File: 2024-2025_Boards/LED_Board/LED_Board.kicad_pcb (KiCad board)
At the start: 2 copper layers, 40 parts, among them J1 Conn_01x02_Socket, J2 Conn_01x02_Socket, J3 Conn_ARM_JTAG_SWD_10, J4 Conn_01x03_Socket, J5 Conn_01x03_Socket, J6 Conn_01x02_Pin, J7 Conn_01x02_Pin, U1 AMS1117-5.0, U2 AMS1117-3.3, U3 MCP2562-E-P, U4 STM32G474RETx

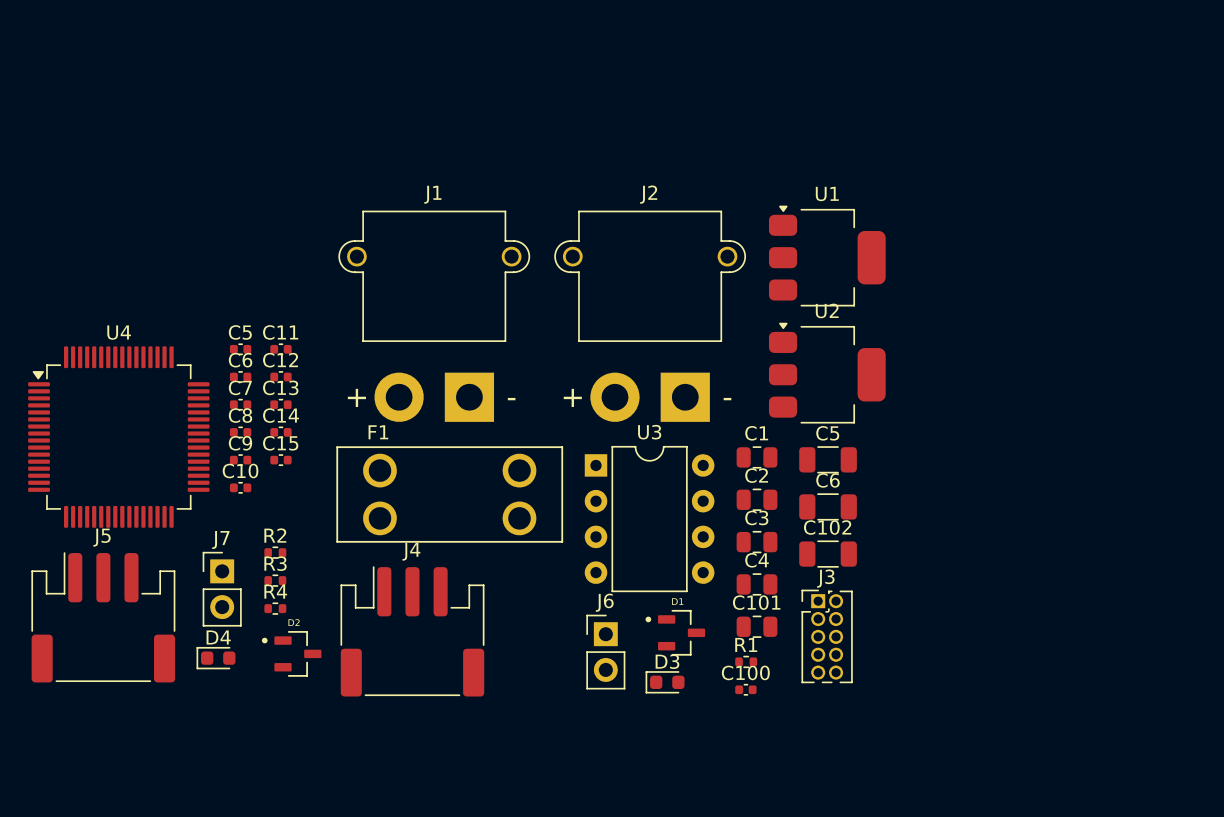
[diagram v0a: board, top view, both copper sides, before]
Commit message: Replaced footprints and new power/can connector
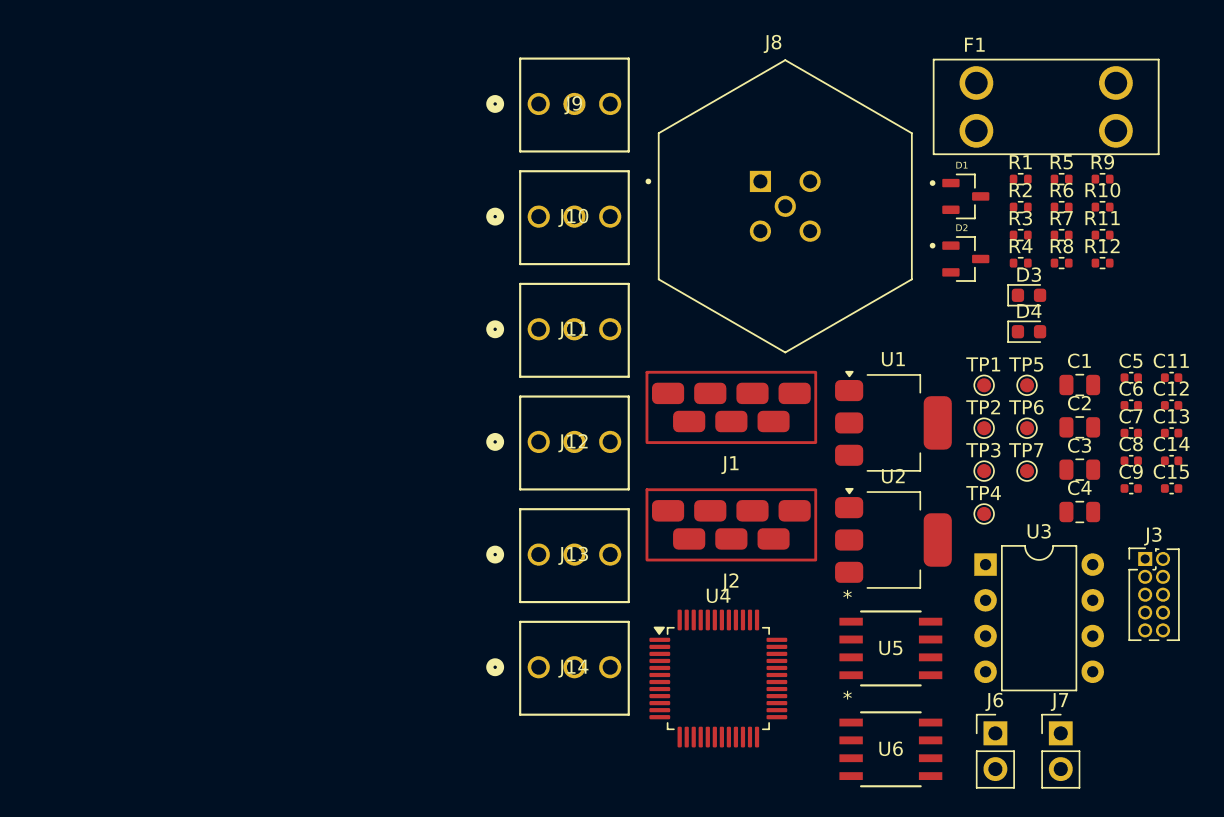
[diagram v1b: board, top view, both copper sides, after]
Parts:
- removed C10: 100nF, Capacitor_SMD:C_0402_1005Metric
- removed C100: 100n, Capacitor_SMD:C_0402_1005Metric
- removed C101: 22u, Capacitor_SMD:C_0805_2012Metric
- removed C102: 47u, Capacitor_SMD:C_1206_3216Metric
- removed the C5 at (112.9, 72.9)
- removed the C5 at (71.2, 65.0)
- removed the C6 at (71.2, 67.0)
- removed the C6 at (112.9, 76.2)
- removed J4, J5: Conn_01x03_Socket, Connector_JST:JST_PH_S3B-PH-SM4-TB_1x03-1MP_P2.00mm_Horizontal
- added C5: 100n, Capacitor_SMD:C_0402_1005Metric, F.Cu at (134.5, 67.0)
- added C6: 100n, Capacitor_SMD:C_0402_1005Metric, F.Cu at (134.5, 69.0)
- added J10: 22232031, CMR_Fan_Pin_Header:CONN_A-6373-03A_MOL, F.Cu at (92.4, 55.6)
- added J11: 22232031, CMR_Fan_Pin_Header:CONN_A-6373-03A_MOL, F.Cu at (92.4, 63.6)
- added J12: 22232031, CMR_Fan_Pin_Header:CONN_A-6373-03A_MOL, F.Cu at (92.4, 71.6)
- added J13: 22232031, CMR_Fan_Pin_Header:CONN_A-6373-03A_MOL, F.Cu at (92.4, 79.6)
- added J14: 22232031, CMR_Fan_Pin_Header:CONN_A-6373-03A_MOL, F.Cu at (92.4, 87.6)
- added J8: 54-00236, CMR_LED_Array_Pins:TENSILITY_54-00236, F.Cu at (109.9, 54.8)
- added J9: 22232031, CMR_Fan_Pin_Header:CONN_A-6373-03A_MOL, F.Cu at (92.4, 47.6)
- added R10: 1k, Resistor_SMD:R_0402_1005Metric, F.Cu at (132.4, 54.9)
- added R11: 1k, Resistor_SMD:R_0402_1005Metric, F.Cu at (132.4, 56.9)
- added R12: 1k, Resistor_SMD:R_0402_1005Metric, F.Cu at (132.4, 58.9)
- added R5: 1k, Resistor_SMD:R_0402_1005Metric, F.Cu at (129.5, 52.9)
- added R6: 1k, Resistor_SMD:R_0402_1005Metric, F.Cu at (129.5, 54.9)
- added R7: 1k, Resistor_SMD:R_0402_1005Metric, F.Cu at (129.5, 56.9)
- added R8: 1k, Resistor_SMD:R_0402_1005Metric, F.Cu at (129.5, 58.9)
- added R9: 1k, Resistor_SMD:R_0402_1005Metric, F.Cu at (132.4, 52.9)
- added TP1: TestPoint, TestPoint:TestPoint_Pad_D1.0mm, F.Cu at (124.0, 67.6)
- added TP2: TestPoint, TestPoint:TestPoint_Pad_D1.0mm, F.Cu at (124.0, 70.6)
- added TP3: TestPoint, TestPoint:TestPoint_Pad_D1.0mm, F.Cu at (124.0, 73.7)
- added TP4: TestPoint, TestPoint:TestPoint_Pad_D1.0mm, F.Cu at (124.0, 76.7)
- added TP5: TestPoint, TestPoint:TestPoint_Pad_D1.0mm, F.Cu at (127.1, 67.6)
- added TP6: TestPoint, TestPoint:TestPoint_Pad_D1.0mm, F.Cu at (127.1, 70.6)
- added TP7: TestPoint, TestPoint:TestPoint_Pad_D1.0mm, F.Cu at (127.1, 73.7)
- added U5: CSD88537ND, CMR_N_Channel_Power_Mosfet:CSD88537ND8-M, F.Cu at (117.4, 86.3)
- added U6: CSD88537ND, CMR_N_Channel_Power_Mosfet:CSD88537ND8-M, F.Cu at (117.4, 93.5)
- J1, J2: value Conn_01x02_Socket -> 3007W2PAT73A10X; footprint Connector_AMASS:AMASS_XT30PW-M_1x02_P2.50mm_Horizontal -> CMR_Power_CAN_Connector:3007W2PAT73A10X
- U4: value STM32G474RETx -> STM32G431CBT6; footprint Package_QFP:LQFP-64_10x10mm_P0.5mm -> Package_QFP:LQFP-48_7x7mm_P0.5mm
- moved C11 63.4 mm to (137.4, 67.0)
- moved C12 63.4 mm to (137.4, 69.0)
- moved C13 63.4 mm to (137.4, 71.0)
- moved C14 63.4 mm to (137.4, 72.9)
- moved C15 63.4 mm to (137.4, 74.9)
- moved C7 63.4 mm to (134.5, 71.0)
- moved C8 63.4 mm to (134.5, 72.9)
- moved C9 63.4 mm to (134.5, 74.9)
- moved D4 62.1 mm to (127.2, 63.8)
- moved J7 60.7 mm to (129.5, 92.3)
- moved R2 58.4 mm to (126.6, 54.9)
- moved R3 58.4 mm to (126.6, 56.9)
- moved R4 58.4 mm to (126.6, 58.9)
- moved D2 55.2 mm to (122.7, 58.6)
- moved F1 50.6 mm to (128.4, 47.8)
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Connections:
- D1 pad 1: CAN_H -> GND
- D1 pad 2: GND -> CAN_H
- D2 pad 1: CAN_L -> GND
- D2 pad 2: GND -> CAN_L
- J1 pad 1: V_IN -> unconnected-(J1-Pad1)
- J1 pad 2: GND -> CAN_L
- J2 pad 1: V_IN -> unconnected-(J2-Pad1)
- J2 pad 2: GND -> CAN_L
- U4 pad 11: unconnected-(U4-PC3-Pad11) -> G1
- U4 pad 12: LED_Debug -> G2
- U4 pad 13: unconnected-(U4-PA1-Pad13) -> G3
- U4 pad 14: unconnected-(U4-PA2-Pad14) -> G4
- U4 pad 15: GND -> unconnected-(U4-PA7-Pad15)
- U4 pad 16: 3.3V -> unconnected-(U4-PB0-Pad16)
- U4 pad 19: unconnected-(U4-PA5-Pad19) -> GND
- U4 pad 20: unconnected-(U4-PA6-Pad20) -> Net-(U4-VREF+)
- U4 pad 21: unconnected-(U4-PA7-Pad21) -> 3.3V
- U4 pad 23: unconnected-(U4-PC5-Pad23) -> GND
- U4 pad 24: unconnected-(U4-PB0-Pad24) -> 3.3V
- U4 pad 27: GND -> unconnected-(U4-PB13-Pad27)
- U4 pad 28: Net-(U4-VREF+) -> unconnected-(U4-PB14-Pad28)
- U4 pad 29: 3.3V -> unconnected-(U4-PB15-Pad29)
- U4 pad 31: GND -> unconnected-(U4-PA9-Pad31)
- U4 pad 32: 3.3V -> unconnected-(U4-PA10-Pad32)
- U4 pad 33: unconnected-(U4-PB11-Pad33) -> CAN_RX
- U4 pad 34: unconnected-(U4-PB12-Pad34) -> CAN_TX
- U4 pad 35: unconnected-(U4-PB13-Pad35) -> GND
- U4 pad 36: unconnected-(U4-PB14-Pad36) -> 3.3V
- U4 pad 37: unconnected-(U4-PB15-Pad37) -> SWDIO
- U4 pad 38: unconnected-(U4-PC6-Pad38) -> SWCLK
- U4 pad 40: unconnected-(U4-PC8-Pad40) -> Net-(U4-PB3)
- U4 pad 45: CAN_RX -> BOOT0
- U4 pad 9: unconnected-(U4-PC1-Pad9) -> LED_Debug

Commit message: New connector and board layout progress
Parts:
- removed J8: 54-00236, CMR_LED_Array_Pins:TENSILITY_54-00236
- added J4: Conn_ARM_JTAG_SWD_10, Connector_PinHeader_1.27mm:PinHeader_2x05_P1.27mm_Vertical, F.Cu at (90.5, 104.2)
- added J5: Conn_01x02_Pin, Connector_PinHeader_2.54mm:PinHeader_1x02_P2.54mm_Vertical, F.Cu at (169.5, 130.1)
- C5, C6: value 100n -> 1u
- J2: value 3007W2PAT73A10X -> Conn_01x02_Socket; footprint CMR_Power_CAN_Connector:3007W2PAT73A10X -> Connector_AMASS:AMASS_XT30PW-M_1x02_P2.50mm_Horizontal
- J3: value Conn_ARM_JTAG_SWD_10 -> Conn_01x03_Socket; footprint Connector_PinHeader_1.27mm:PinHeader_2x05_P1.27mm_Vertical -> Connector_JST:JST_PH_S3B-PH-SM4-TB_1x03-1MP_P2.00mm_Horizontal
- J7: value Conn_01x02_Pin -> 54-00236; footprint Connector_PinHeader_2.54mm:PinHeader_1x02_P2.54mm_Vertical -> CMR_LED_Array_Pins:TENSILITY_54-00236
- U3: value MCP2562-E-P -> TCAN1057AEV-Q1; footprint Package_DIP:DIP-8_W7.62mm -> Package_SO:SOIC-8_3.9x4.9mm_P1.27mm
- moved F1 83.5 mm to (129.8, 131.2), turned to -90 degrees
- moved J10 76.7 mm to (145.8, 110.6), turned to 90 degrees
- moved J9 76.2 mm to (145.8, 102.0), turned to 90 degrees
- moved J2 76.2 mm to (144.5, 147.8)
- moved TP1 74.5 mm to (182.9, 113.2)
- moved TP5 74.5 mm to (186.0, 113.2)
- moved TP6 74.5 mm to (186.0, 116.2)
- moved TP7 74.5 mm to (186.0, 119.3)
- moved TP2 74.5 mm to (182.9, 116.2)
- moved TP3 74.5 mm to (182.9, 119.3)
- moved TP4 74.5 mm to (182.9, 122.3)
- moved C1 71.3 mm to (124.0, 138.5), turned to 180 degrees
- moved C2 69.4 mm to (120.5, 139.2), turned to -90 degrees
- moved C13 68.2 mm to (81.7, 110.4), turned to 180 degrees
- moved D3 67.6 mm to (186.7, 93.3)
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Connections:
- C1 pad 1: Net-(U1-VI) -> V_Fuse
- C5 pad 1: 3.3V -> 5V
- C6 pad 1: GND -> 3.3V
- C6 pad 2: 5V -> GND
- F1 pad 2: Net-(U1-VI) -> V_Fuse
- F1 pad 4: Net-(U1-VI) -> V_Fuse
- J1 pad 1: unconnected-(J1-Pad1) -> CAN_L
- J1 pad 2: CAN_L -> GND
- J1 pad 3: GND -> unconnected-(J1-Pad3)
- J1 pad 4: CAN_H -> unconnected-(J1-Pad4)
- J1 pad 5: unconnected-(J1-Pad5) -> CAN_H
- J2 pad 1: unconnected-(J2-Pad1) -> GND
- J2 pad 2: CAN_L -> V_IN
- J3 pad 1: 3.3V -> CAN_H
- J3 pad 2: SWDIO -> CAN_L
- J6 pad 1: 3.3V -> GND
- J6 pad 2: BOOT0 -> NRST
- J7 pad 1: GND -> LED_1
- J7 pad 2: NRST -> LED_2
- U1 pad 3: Net-(U1-VI) -> V_Fuse
- U4 pad 40: Net-(U4-PB3) -> SWO
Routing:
- net 5V: track 0.00 -> 50.1 mm
- net V_Fuse: track 0.00 -> 10.1 mm
- net 3.3V: track 0.00 -> 9.32 mm
- net GND: track 0.00 -> 4.83 mm, vias 0 -> 1
- net SWDIO: track 0.00 -> 4.77 mm
- net SWCLK: track 0.00 -> 4.68 mm
- net Net-(U4-VREF+): track 0.00 -> 3.04 mm
- net SWO: track 0.00 -> 2.95 mm
- net Net-(U4-PB3): track 0.00 -> 2.27 mm
- added copper zone on B.Cu, net GND
- added copper zone on F.Cu, net V_IN
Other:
- board outline added: 75 x 55 mm

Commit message: PCB Connected
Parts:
- removed J12, J13, J14: 22232031, CMR_Fan_Pin_Header:CONN_A-6373-03A_MOL
- removed TP2, TP4, TP6, TP7: TestPoint, TestPoint:TestPoint_Pad_D1.0mm
- added C10: 100n, Capacitor_SMD:C_0402_1005Metric, F.Cu at (119.8, 116.8)
- added C16: 1u, Capacitor_SMD:C_0402_1005Metric, F.Cu at (112.8, 126.0)
- added C17: 1u, Capacitor_SMD:C_0402_1005Metric, F.Cu at (110.8, 135.0)
- added D5: GREEN, LED_SMD:LED_0603_1608Metric, F.Cu at (115.5, 118.2)
- added D6: GREEN, LED_SMD:LED_0603_1608Metric, F.Cu at (115.5, 120.0)
- added D7: GREEN, LED_SMD:LED_0603_1608Metric, F.Cu at (115.5, 121.8)
- added H1: MountingHole, MountingHole:MountingHole_2.7mm_M2.5, F.Cu at (97.5, 100.5)
- added H2: MountingHole, MountingHole:MountingHole_2.7mm_M2.5, F.Cu at (97.5, 146.0)
- added H3: MountingHole, MountingHole:MountingHole_2.7mm_M2.5, F.Cu at (145.8, 100.5)
- added H4: MountingHole, MountingHole:MountingHole_2.7mm_M2.5, F.Cu at (146.0, 146.0)
- added J8: Conn_01x03_Pin, Cornell_Mars_Rover:CONN_A-7395-03B_MOL, F.Cu at (108.5, 111.4)
- added LED1: TestPoint, TestPoint:TestPoint_Pad_D1.0mm, F.Cu at (129.8, 99.2)
- added LED2: TestPoint, TestPoint:TestPoint_Pad_D1.0mm, F.Cu at (132.0, 106.0)
- added LED3: TestPoint, TestPoint:TestPoint_Pad_D1.0mm, F.Cu at (137.8, 106.0)
- added LED4: TestPoint, TestPoint:TestPoint_Pad_D1.0mm, F.Cu at (130.5, 118.5)
- added R13: 1k, Resistor_SMD:R_0402_1005Metric, F.Cu at (112.5, 116.5)
- added R14: 1k, Resistor_SMD:R_0402_1005Metric, F.Cu at (112.5, 118.2)
- added R15: 1k, Resistor_SMD:R_0402_1005Metric, F.Cu at (112.5, 120.0)
- added R16: 1k, Resistor_SMD:R_0402_1005Metric, F.Cu at (112.5, 121.8)
- C1: value 10u -> 4.7u
- C11, C12, C8: value 100nF -> 100n
- C13: value 100nF -> 1u
- C14: value 4.7uF -> 4.7u
- C15: value 2.2uF -> 2.2u
- C2: value 22u -> 100n; footprint Capacitor_SMD:C_0805_2012Metric -> Capacitor_SMD:C_0402_1005Metric
- C3, C4: value 10u -> 22u
- C6: value 1u -> 10u; footprint Capacitor_SMD:C_0402_1005Metric -> Capacitor_SMD:C_0805_2012Metric
- C7: value 100n -> 22u; footprint Capacitor_SMD:C_0402_1005Metric -> Capacitor_SMD:C_0805_2012Metric
- C9: value 1uF -> 100n
- D1, D2: footprint CMR_Voltage_Suppressor:SOT95P237X111-3N -> Cornell_Mars_Rover:SOT95P237X111-3N
- D3: value GREEN -> RED
- F1: footprint CMR_Fuse:FUSE_3568 -> Cornell_Mars_Rover:FUSE_3568
- J1: value 3007W2PAT73A10X -> Conn_02x10_Odd_Even; footprint CMR_Power_CAN_Connector:3007W2PAT73A10X -> Cornell_Mars_Rover:CONN20_D10-RA-BK_SUL
- J10, J11, J9: value 22232031 -> Conn_01x03_Pin; footprint CMR_Fan_Pin_Header:CONN_A-6373-03A_MOL -> Cornell_Mars_Rover:CONN_A-7395-03B_MOL
- J2: value Conn_01x02_Socket -> Conn_01x02_Pin; footprint Connector_AMASS:AMASS_XT30PW-M_1x02_P2.50mm_Horizontal -> Cornell_Mars_Rover:CONN_PH1RB-02-UA_ADM
- J3: value Conn_01x03_Socket -> Conn_01x02_Pin; footprint Connector_JST:JST_PH_S3B-PH-SM4-TB_1x03-1MP_P2.00mm_Horizontal -> Cornell_Mars_Rover:CONN_PH1RB-02-UA_ADM
- J5: value Conn_01x02_Pin -> Conn_01x05_Pin; footprint Connector_PinHeader_2.54mm:PinHeader_1x02_P2.54mm_Vertical -> Cornell_Mars_Rover:CONN05_GRPB051VWCN-RC_SUL
- J6: value Conn_01x02_Pin -> Conn_01x03_Pin; footprint Connector_PinHeader_2.54mm:PinHeader_1x02_P2.54mm_Vertical -> Cornell_Mars_Rover:CONN_A-7395-03B_MOL
- J7: value 54-00236 -> Conn_01x03_Pin; footprint CMR_LED_Array_Pins:TENSILITY_54-00236 -> Cornell_Mars_Rover:CONN_A-7395-03B_MOL
- R1: value 10k -> 40.2k; footprint Resistor_SMD:R_0402_1005Metric -> Resistor_SMD:R_0603_1608Metric
- R2: value 1k -> 10k; footprint Resistor_SMD:R_0402_1005Metric -> Resistor_SMD:R_0603_1608Metric
- R3: value 1k -> 10k
- R4: value 0 -> 1k
- U1: value AMS1117-5.0 -> TLVM23625RDNR; footprint Package_TO_SOT_SMD:SOT-223-3_TabPin2 -> Cornell_Mars_Rover:RDN0011A-MFG
- U3: value TCAN1057AEV-Q1 -> STM32G431CBT6; footprint Package_SO:SOIC-8_3.9x4.9mm_P1.27mm -> Package_QFP:LQFP-48_7x7mm_P0.5mm
- U4: value STM32G431CBT6 -> TCAN1057AEV-Q1; footprint Package_QFP:LQFP-48_7x7mm_P0.5mm -> Package_SO:SOIC-8_3.9x4.9mm_P1.27mm
- U5, U6: footprint CMR_N_Channel_Power_Mosfet:CSD88537ND8-M -> Cornell_Mars_Rover:CSD88537ND8-M
- moved D4 74.1 mm to (115.5, 116.5)
- moved D1 67.5 mm to (118.0, 129.8)
- moved D2 67.0 mm to (118.2, 133.8)
- moved R3 61.3 mm to (124.3, 127.8), turned to 180 degrees
- moved R2 56.8 mm to (131.6, 128.8), turned to -90 degrees
- moved R1 53.8 mm to (134.8, 126.0), turned to 180 degrees
- moved R11 53.6 mm to (131.5, 111.4), turned to 180 degrees
- moved R10 53.4 mm to (131.5, 108.9), turned to 180 degrees
- moved R9 51.9 mm to (132.0, 102.1), turned to 180 degrees
- moved J6 51.2 mm to (126.5, 111.4), turned to 180 degrees
- moved R7 51.1 mm to (131.5, 112.7)
- moved R6 51.0 mm to (131.5, 110.2)
- moved R5 49.3 mm to (132.0, 103.3)
- moved J11 48.6 mm to (102.7, 135.1), turned to 0 degrees
- moved R8 48.2 mm to (132.0, 99.6), turned to 180 degrees
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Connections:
- C11 pad 1: GND -> 3.3V
- C11 pad 2: 3.3V -> GND
- C12 pad 1: GND -> Net-(U3-VREF+)
- C12 pad 2: 3.3V -> GND
- C13 pad 1: 3.3V -> Net-(U3-VREF+)
- C2 pad 1: 5V -> V_Fuse
- C4 pad 1: 3.3V -> 5V
- C5 pad 1: 5V -> VCC
- C6 pad 1: 3.3V -> 5V
- C7 pad 1: NRST -> 3.3V
- C8 pad 1: Net-(U4-VREF+) -> NRST
- C9 pad 1: Net-(U4-VREF+) -> 3.3V
- D1 pad 2: CAN_H -> CAN+
- D2 pad 2: CAN_L -> CAN-
- D4 pad 2: LED_Debug -> LED_Debug1
- J1 pad 1: CAN_L -> CAN+
- J1 pad 2: GND -> CAN-
- J1 pad 3: unconnected-(J1-Pad3) -> NRST
- J1 pad 4: unconnected-(J1-Pad4) -> GND
- J1 pad 5: CAN_H -> GND
- J10 pad 1: GND -> 5V
- J10 pad 2: 5V -> unconnected-(J10-Pin_2-Pad2)
- J10 pad 3: unconnected-(J10-Pad3) -> GND
- J11 pad 1: GND -> 5V
- J11 pad 2: 5V -> unconnected-(J11-Pin_2-Pad2)
- J11 pad 3: unconnected-(J11-Pad3) -> GND
- J2 pad 1: GND -> 3.3V
- J2 pad 2: V_IN -> BOOT0
- J3 pad 1: CAN_H -> GND
- J3 pad 2: CAN_L -> NRST
- J5 pad 1: 3.3V -> LED_4
- J5 pad 2: BOOT0 -> LED_3
- J6 pad 1: GND -> 5V
- J6 pad 2: NRST -> unconnected-(J6-Pin_2-Pad2)
- J7 pad 1: LED_1 -> 5V
- J7 pad 2: LED_2 -> unconnected-(J7-Pin_2-Pad2)
- J7 pad 3: V_Fuse -> GND
- J9 pad 1: GND -> 5V
- J9 pad 2: 5V -> unconnected-(J9-Pin_2-Pad2)
- J9 pad 3: unconnected-(J9-Pad3) -> GND
- R1 pad 1: BOOT0 -> 5V
- R1 pad 2: GND -> Net-(U1-FB)
- R10 pad 1: G4 -> Net-(U6-G1)
- R10 pad 2: Net-(U6-G2) -> GND
- R11 pad 1: Net-(U6-G1) -> Net-(U6-G2)
- R12 pad 1: Net-(U6-G2) -> Net-(D3-K)
- R2 pad 1: Net-(D3-K) -> Net-(U1-FB)
- R3 pad 1: Net-(D4-K) -> BOOT0
- R4 pad 1: Net-(U4-PB3) -> G1
- R4 pad 2: SWO -> Net-(U5-G1)
- R5 pad 1: G1 -> G2
- R5 pad 2: Net-(U5-G1) -> Net-(U5-G2)
- R6 pad 1: G2 -> G3
- R6 pad 2: Net-(U5-G2) -> Net-(U6-G1)
- R7 pad 1: Net-(U5-G1) -> G4
- R7 pad 2: GND -> Net-(U6-G2)
- R8 pad 1: Net-(U5-G2) -> Net-(U5-G1)
- R9 pad 1: G3 -> Net-(U5-G2)
- R9 pad 2: Net-(U6-G1) -> GND
- TP3 pad 1: 3.3V -> 5V
- TP5 pad 1: G2 -> 3.3V
- U1 pad 1: GND -> unconnected-(U1-PGOOD-Pad1)
- U1 pad 2: 5V -> V_Fuse
- U3 pad 1: CAN_TX -> 3.3V
- U3 pad 2: GND -> unconnected-(U3-PC13-Pad2)
- U3 pad 3: 5V -> unconnected-(U3-PC14-Pad3)
- U3 pad 4: CAN_RX -> unconnected-(U3-PC15-Pad4)
- U3 pad 5: 3.3V -> unconnected-(U3-PF0-Pad5)
- U3 pad 6: CAN_L -> unconnected-(U3-PF1-Pad6)
- U3 pad 7: CAN_H -> NRST
- U3 pad 8: GND -> unconnected-(U3-PA0-Pad8)
- U4 pad 1: 3.3V -> CAN_TX
- U4 pad 2: unconnected-(U4-PC13-Pad2) -> GND
- U4 pad 3: unconnected-(U4-PC14-Pad3) -> 5V
- U4 pad 4: unconnected-(U4-PC15-Pad4) -> CAN_RX
- U4 pad 5: unconnected-(U4-PF0-Pad5) -> 3.3V
- U4 pad 6: unconnected-(U4-PF1-Pad6) -> CAN-
- U4 pad 7: NRST -> CAN+
- U4 pad 8: unconnected-(U4-PA0-Pad8) -> GND
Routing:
- net 5V: track 50.1 -> 124.0 mm, vias 0 -> 1
- net 3.3V: track 9.32 -> 80.9 mm, vias 0 -> 1
- net GND: track 4.83 -> 65.3 mm, vias 1 -> 25
- net NRST: track 0.00 -> 49.0 mm, vias 0 -> 1
- net V_IN: track 0.00 -> 29.8 mm
- net V_Fuse: track 10.1 -> 37.5 mm
- net BOOT0: track 0.00 -> 25.0 mm, vias 0 -> 1
- net G3: track 0.00 -> 21.9 mm
- net G1: track 0.00 -> 21.5 mm
- net G2: track 0.00 -> 17.4 mm
- net CAN-: track 0.00 -> 14.2 mm
- net Net-(U1-FB): track 0.00 -> 13.7 mm, vias 0 -> 2
- net CAN_RX: track 0.00 -> 11.9 mm
- net CAN+: track 0.00 -> 11.8 mm
- net G4: track 0.00 -> 8.97 mm
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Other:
- board size 75 x 55 mm -> 56.5 x 53.5 mm
- board text added: "1"
- board text added: "2"
- board text added: "3"
- board text added: "3.3V"
- board text added: "4"
- board text added: "BOOT"
- board text added: "GND"
- board text added: "NRST"
- board text added: "VIN"

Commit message: Pins on correct side
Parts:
- J2, J3: footprint Cornell_Mars_Rover:CONN_PH1RB-02-UA_ADM -> Connector_PinHeader_2.54mm:PinHeader_1x02_P2.54mm_Horizontal
- J5: footprint Cornell_Mars_Rover:CONN05_GRPB051VWCN-RC_SUL -> Connector_JST:JST_EH_S5B-EH_1x05_P2.50mm_Horizontal
- moved TP3 101.8 mm to (105.0, 117.8), turned to 180 degrees
- moved TP1 101.0 mm to (100.0, 117.8), turned to 180 degrees
- moved TP5 72.1 mm to (130.0, 135.8)
- moved J5 54.3 mm to (97.3, 136.2)
- moved D3 47.4 mm to (119.3, 142.2), turned to 180 degrees
- moved U5 45.5 mm to (108.8, 136.8), turned to 180 degrees
- moved TP2 44.2 mm to (113.8, 140.4)
- moved R8 43.0 mm to (114.2, 138.7), turned to 0 degrees
- moved R12 42.5 mm to (122.3, 142.2), turned to 0 degrees
- moved R4 40.7 mm to (114.2, 137.4), turned to 180 degrees
- moved TP6 39.8 mm to (108.0, 132.5), turned to 180 degrees
- moved R9 38.5 mm to (114.2, 136.2), turned to 0 degrees
- moved R5 36.3 mm to (114.2, 134.9), turned to 180 degrees
- moved U6 33.2 mm to (108.8, 128.2), turned to 180 degrees
- moved TP4 32.5 mm to (114.2, 133.2), turned to 180 degrees
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- renumbered LED1 to TP2, LED2 to TP4, LED3 to TP6, LED4 to TP7
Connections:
- J5 pad 1: LED_4 -> V_IN
- J5 pad 2: LED_3 -> LED_1
- J5 pad 3: V_Fuse -> LED_2
- J5 pad 4: LED_2 -> LED_3
- J5 pad 5: LED_1 -> LED_4
- U3 pad 11: G4 -> LED_Debug4
- U3 pad 12: G3 -> LED_Debug3
- U3 pad 13: G2 -> LED_Debug2
- U3 pad 14: G1 -> LED_Debug1
- U3 pad 26: LED_Debug1 -> G4
- U3 pad 27: LED_Debug2 -> G3
- U3 pad 28: LED_Debug3 -> G2
- U3 pad 29: LED_Debug4 -> G1
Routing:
- net 3.3V: track 80.9 -> 108.5 mm, vias 1 -> 2
- net V_Fuse: track 37.5 -> 12.5 mm
- net CAN_RX: track 11.9 -> 26.8 mm, vias 0 -> 2
- net CAN_TX: track 7.73 -> 22.3 mm, vias 0 -> 2
- net V_IN: track 29.8 -> 42.2 mm
- net G2: track 17.4 -> 7.98 mm
- net GND: track 65.3 -> 72.4 mm, vias 25 -> 35
- net G3: track 21.9 -> 15.3 mm
- net 5V: track 124.0 -> 117.6 mm
- net G1: track 21.5 -> 15.9 mm
- net LED_2: track 7.20 -> 11.4 mm
- net LED_1: track 7.73 -> 11.4 mm
- net LED_3: track 6.51 -> 9.97 mm
- net LED_Debug4: track 3.70 -> 7.10 mm
- net LED_4: track 6.88 -> 9.95 mm
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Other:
- board size 56.5 x 53.5 mm -> 60 x 37.5 mm

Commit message: PCB Finished
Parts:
- added G***: LOGO, Cornell_Mars_Rover:CMR_Logo, F.Cu at (104.5, 120.5)
- moved R3 20.8 mm to (123.5, 134.8), turned to 180 degrees
- moved 5V 17.5 mm to (122.5, 118.0)
- moved GND 17.5 mm to (117.5, 118.0)
- moved LED1 4.08 mm to (116.0, 137.0)
- moved LED4 3.91 mm to (116.5, 121.0)
- moved LED2 3.09 mm to (113.5, 130.2)
- moved R10 3.00 mm to (114.4, 127.1)
- moved R6 3.00 mm to (114.4, 125.8)
- moved R11 3.00 mm to (114.4, 124.6)
- moved R7 3.00 mm to (114.4, 123.3)
- moved U6 3.00 mm to (108.8, 125.2)
- moved LED3 2.37 mm to (107.2, 130.2)
- moved C10 2.00 mm to (118.5, 123.6)
- moved C11 2.00 mm to (126.5, 133.5)
- moved C12 2.00 mm to (122.5, 121.2)
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- renumbered TP3 to 5V, TP1 to GND, TP2 to LED1, TP4 to LED2, TP6 to LED3, TP7 to LED4
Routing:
- net GND: track 72.4 -> 82.2 mm, vias 35 -> 37
- net G1: track 15.9 -> 12.5 mm
- net 3.3V: track 108.5 -> 111.1 mm
- net 5V: track 117.6 -> 120.2 mm
- net NRST: track 47.4 -> 49.8 mm
- net G4: track 6.42 -> 8.67 mm
- net BOOT0: track 24.8 -> 26.5 mm
- net LED_2: track 11.4 -> 9.93 mm
- net LED_1: track 11.4 -> 9.94 mm
- net CAN_TX: track 22.3 -> 23.5 mm
- net G2: track 7.98 -> 9.15 mm
- net SWO: track 3.52 -> 4.65 mm
- net SWCLK: track 3.63 -> 4.73 mm
- net SWDIO: track 3.95 -> 5.05 mm
- net G3: track 15.3 -> 16.4 mm
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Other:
- board text added: "2025"
- board text added: "Dawson Melton"
